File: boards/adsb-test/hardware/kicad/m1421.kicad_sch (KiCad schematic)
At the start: 35 parts, among them J1401 m1421 JTAG (J-Link), J1402 ADSBee 1421 Dev Kit, J1403 SMA 1090/978, U1401 ADSBee m1421, U1402 74LVC1G97 (AND), U1403 74LVC1G32, U1404 74LVC1G07, U1405 SCN-2-11+

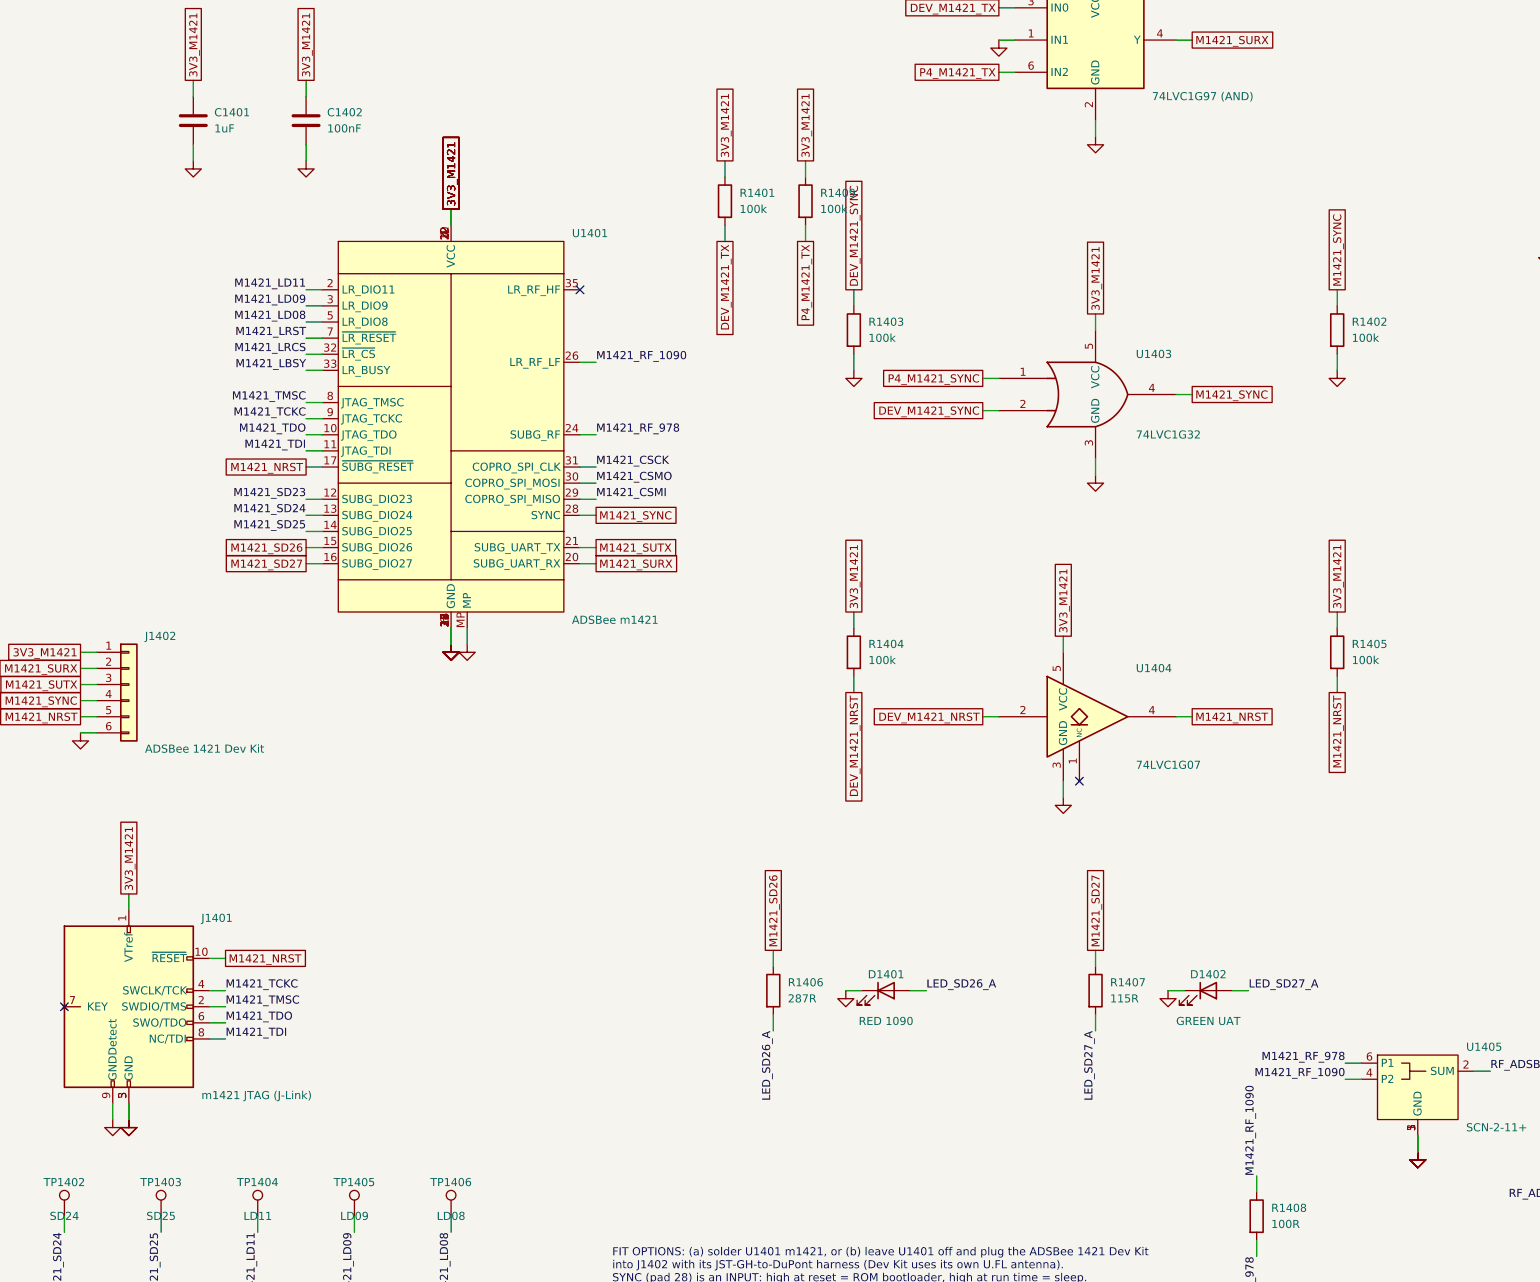
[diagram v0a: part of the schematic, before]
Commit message: Schematic generator: hide stacked pins (KiCad convention) so pin numbers don't overprint
Co-Authored-By: Claude Opus 5.5 <noreply@anthropic.com>
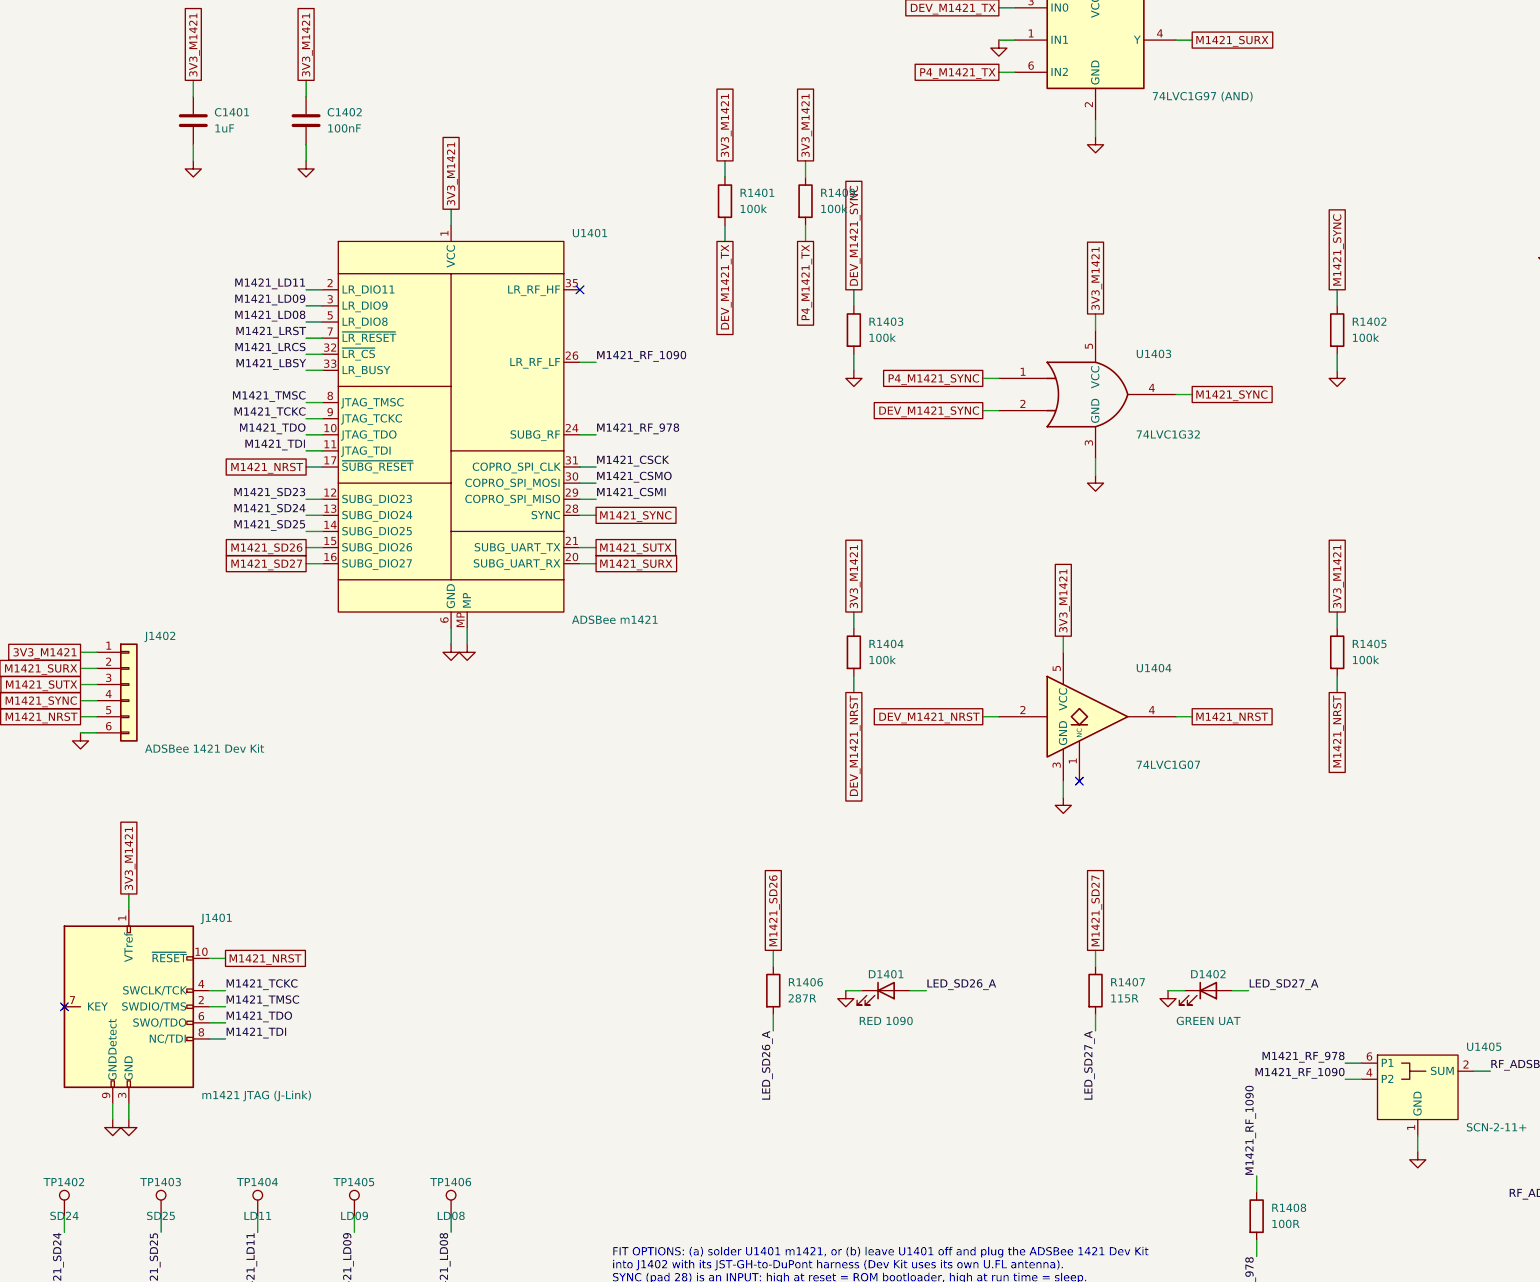
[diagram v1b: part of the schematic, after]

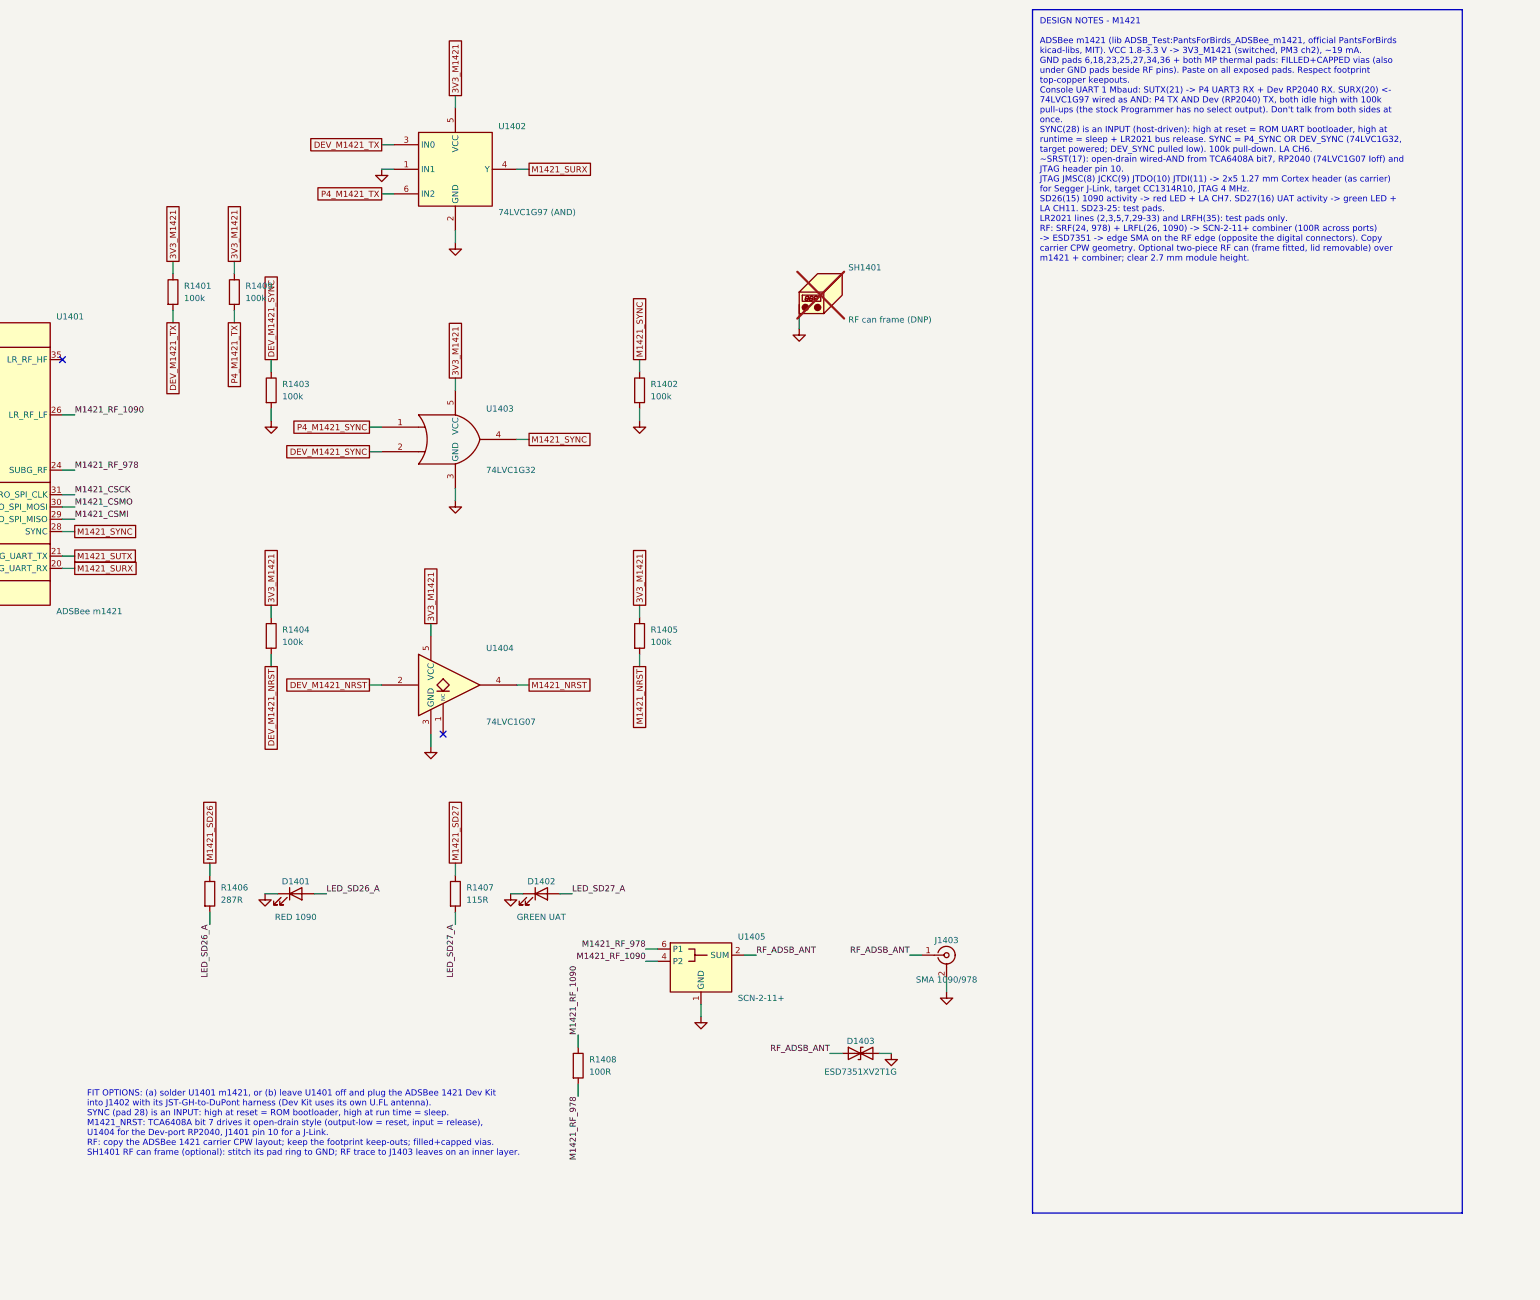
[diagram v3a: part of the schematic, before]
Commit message: ADSB_Test: Dev port split over three A3 sheets; old note boxes replaced with short current notes
Co-Authored-By: Claude Opus 5.5 <noreply@anthropic.com>
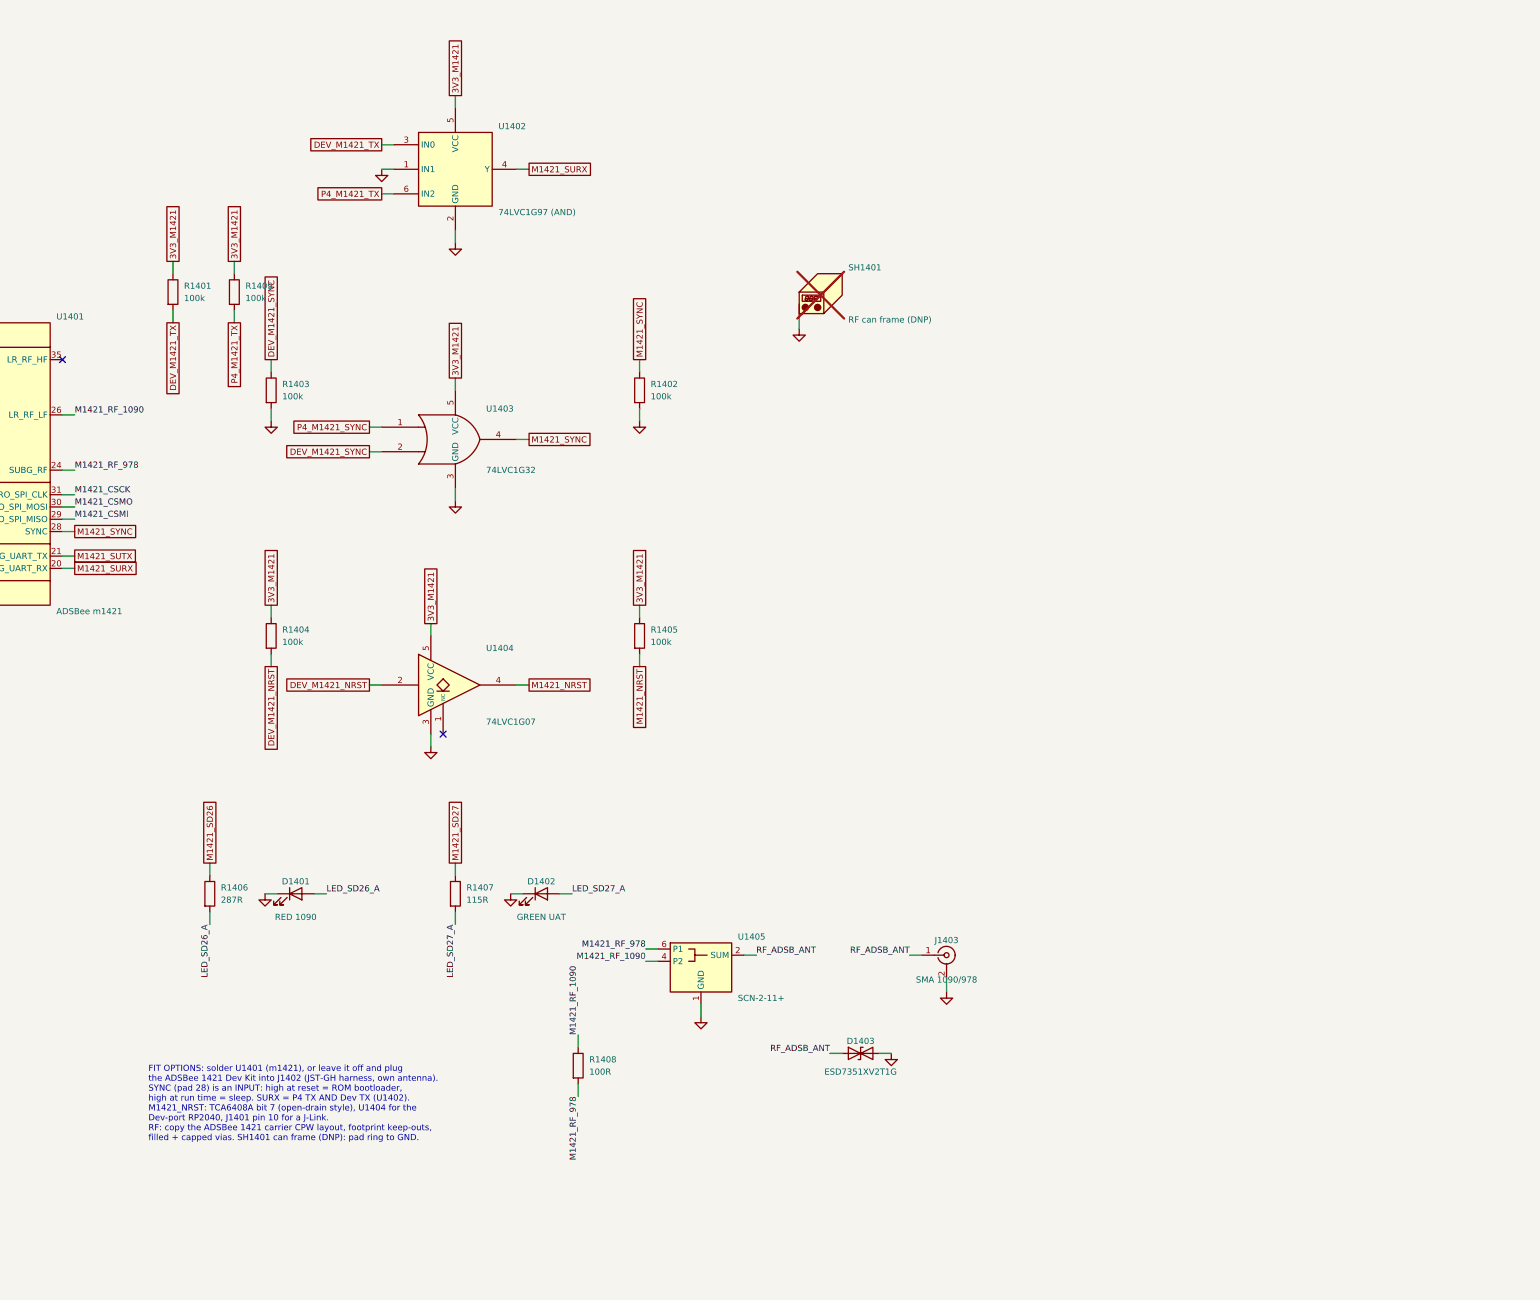
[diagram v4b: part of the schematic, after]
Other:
- note added: "FIT OPTIONS: solder U1401 (m1421), or leave it off and plug the ADSBee 1421 Dev Kit into J1402 (JST-GH harness, own antenna). SYNC (pad 28) is an INPUT: high at reset = ROM bootloader, high at run time = sleep. SURX = P4 TX AND Dev TX (U1402). M1421_NRST: TCA6408A bit 7 (open-drain style), U1404 for the Dev-port RP2040, J1401 pin 10 for a J-Link. RF: copy the ADSBee 1421 carrier CPW layout, footp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"
- note removed: "FIT OPTIONS: (a) solder U1401 m1421, or (b) leave U1401 off and plug the ADSBee 1421 Dev Kit into J1402 with its JST-GH-to-DuPont harness (Dev Kit uses its own U.FL antenna). SYNC (pad 28) is an INPUT: high at reset = ROM bootloader, high at run time = sleep. M1421_NRST: TCA6408A bit 7 drives it open-drain style (output-low = reset, input = release), U1404 for the Dev-port RP2040, J1401 pin 10 fo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"
